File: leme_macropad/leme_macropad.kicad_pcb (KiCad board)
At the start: 4 copper layers, 99.9 x 63.9 mm, 90 parts, among them J1 OLED display, J2 USB_C_Receptacle_USB2.0_16P, SW1 SW_Push, SW2 SW_Push, SW3 SW_Push, SW4 RotaryEncoder_Switch, SW5 SW_Push, SW6 SW_Push, SW7 SW_Push, SW8 SW_Push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

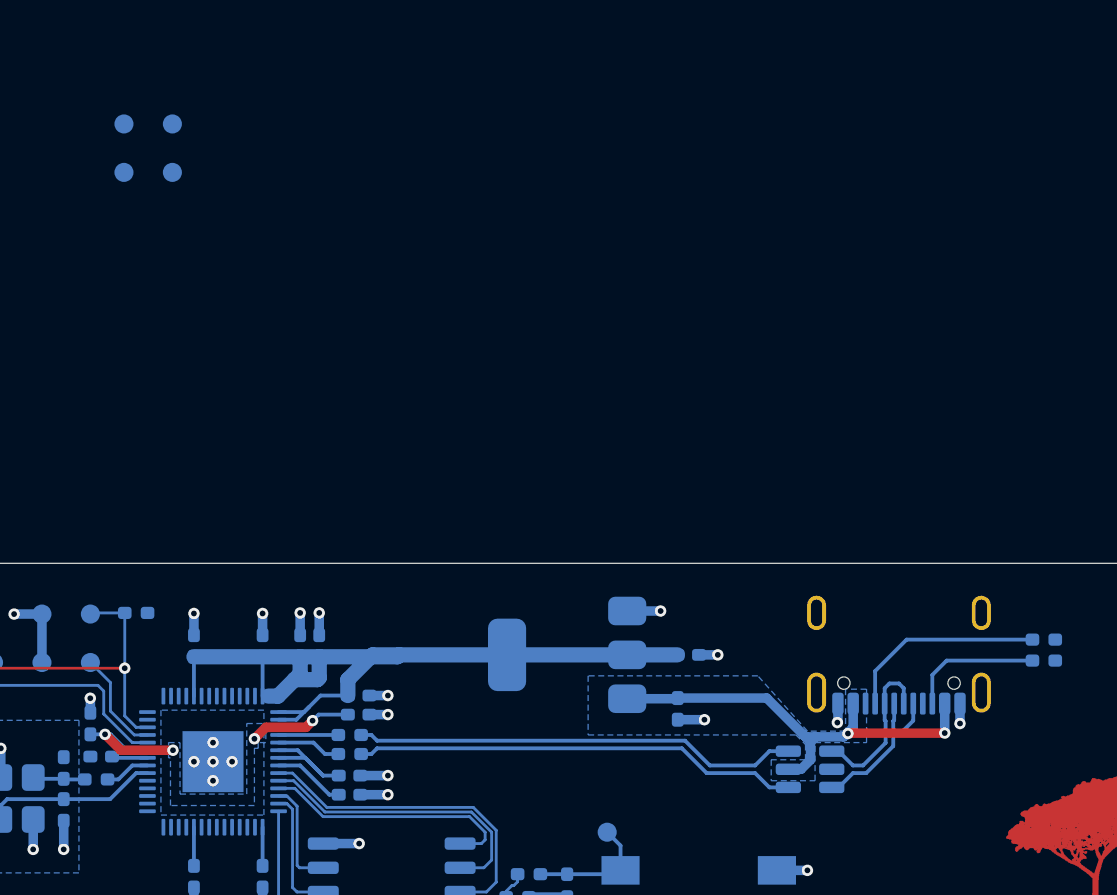
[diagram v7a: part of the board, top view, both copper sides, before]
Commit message: Routes power testpoints
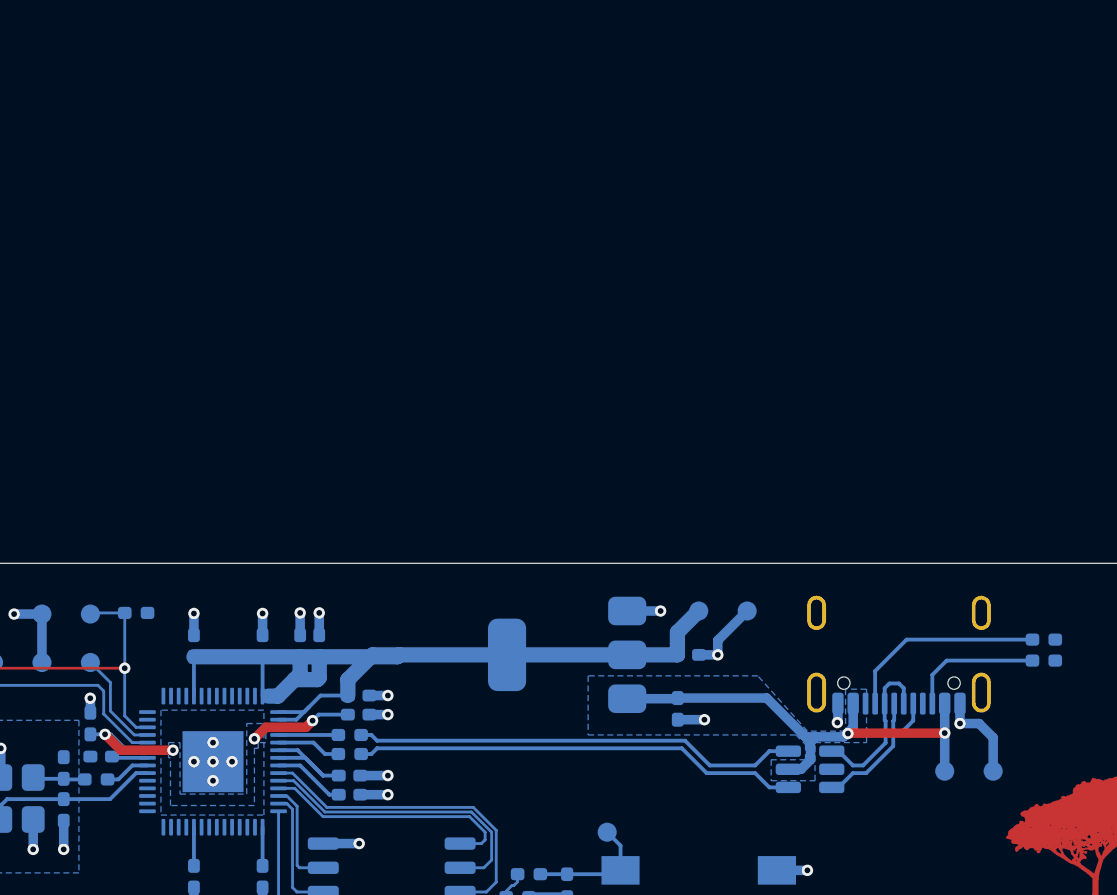
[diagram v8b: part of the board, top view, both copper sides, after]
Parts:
- moved TP4 54.8 mm to (173.8, 75.9)
- moved TP3 54.8 mm to (176.3, 75.9)
- moved TP6 37.9 mm to (160.9, 67.5)
- moved TP5 37.9 mm to (163.4, 67.5)
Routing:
- net GND: track 34.8 -> 41.5 mm
- net +3.3V: track 61.7 -> 64.5 mm
- net +5V: track 24.0 -> 26.0 mm
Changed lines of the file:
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@@
 	(footprint "TestPoint:TestPoint_Pad_D1.0mm"
 		(layer "B.Cu")
-		(at 130.76 44.5 180)
+		(at 160.9 67.5 180)
 		(descr "SMD pad as test Point, diameter 1.0mm")
 		(tags "test point SMD pad")
@@
 	(footprint "TestPoint:TestPoint_Pad_D1.0mm"
 		(layer "B.Cu")
-		(at 130.76 41.96 180)
+		(at 173.8 75.9 180)
 		(descr "SMD pad as test Point, diameter 1.0mm")
 		(tags "test point SMD pad")
@@
 	(footprint "TestPoint:TestPoint_Pad_D1.0mm"
 		(layer "B.Cu")
-		(at 133.3 41.96 180)
+		(at 176.34 75.9 180)
 		(descr "SMD pad as test Point, diameter 1.0mm")
 		(tags "test point SMD pad")
@@
 	(footprint "TestPoint:TestPoint_Pad_D1.0mm"
 		(layer "B.Cu")
-		(at 133.3 44.5 180)
+		(at 163.44 67.5 180)
 		(descr "SMD pad as test Point, diameter 1.0mm")
 		(tags "test point SMD pad")
@@
 	)
 	(segment
+		(start 173.8 73.9)
+		(end 173.8 75.9)
+		(width 0.5)
+		(layer "B.Cu")
+		(net 1)
+	)
+	(segment
 		(start 166.262499 75.8)
 		(end 165.6 75.8)
@@
 	)
 	(segment
+		(start 161.9 69.8)
+		(end 161.9 69.04)
+		(width 0.5)
+		(layer "B.Cu")
+		(net 2)
+	)
+	(segment
 		(start 141 68.765)
 		(end 141 67.6)
@@
 	)
 	(segment
+		(start 175.6 73.4)
+		(end 174.6 73.4)
+		(width 0.5)
+		(layer "B.Cu")
+		(net 2)
+	)
+	(segment
 		(start 140 68.765)
 		(end 140 67.6)
@@
 	)
 	(segment
+		(start 176.34 75.9)
+		(end 176.34 74.14)
+		(width 0.5)
+		(layer "B.Cu")
+		(net 2)
+	)
+	(segment
 		(start 129 72.081587)
 		(end 128.993413 72.075)
@@
 	)
 	(segment
+		(start 161.9 69.04)
+		(end 163.44 67.5)
+		(width 0.5)
+		(layer "B.Cu")
+		(net 2)
+	)
+	(segment
 		(start 135.43 74.43)
 		(end 135.4 74.4)
@@
 	)
 	(segment
+		(start 176.34 74.14)
+		(end 175.6 73.4)
+		(width 0.5)
+		(layer "B.Cu")
+		(net 2)
+	)
+	(segment
 		(start 144.6 76.129937)
 		(end 143.157144 76.129937)
@@
 	)
 	(segment
+		(start 159.7825 68.6175)
+		(end 160.9 67.5)
+		(width 0.8)
+		(layer "B.Cu")
+		(net 3)
+	)
+	(segment
 		(start 138.03 71.9625)
 		(end 138.03 69.9)
@@
 		(width 0.8)
 		(layer "B.Cu")
+		(net 3)
+	)
+	(segment
+		(start 159.7825 69.8)
+		(end 159.7825 68.6175)
+		(width 0.8)
+		(layer "B.Cu")
